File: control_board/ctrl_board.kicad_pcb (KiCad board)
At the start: 2 copper layers, 130 x 130 mm, 37 parts, among them J1 CONN_01X04, J2 CONN_01X02, J3 CONN_01X04, J4 CONN_01X04, J5 CONN_01X04, J6 CONN_01X04, J7 CONN_01X04, J8 CONN_01X04, U1 PCA9685PW, U2 MBI1801, U3 MBI1801, U4 MBI1801, U5 MBI1801, U6 MBI1801, U7 MBI1801

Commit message: ctrl_board: [wip] place and route
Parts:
- C11, C13, C3, C5, C7, C9: value 100n -> 100u
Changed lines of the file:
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@@
     (visible_elements FFFFBF7F)
     (pcbplotparams
-      (layerselection 0x00030_ffffffff)
+      (layerselection 0x010fc_ffffffff)
       (usegerberextensions false)
       (excludeedgelayer true)
-      (linewidth 0.150000)
+      (linewidth 0.020000)
       (plotframeref false)
       (viasonmask false)
@@
       (drillshape 0)
       (scaleselection 1)
-      (outputdirectory ""))
+      (outputdirectory gerbers/))
   )
   (net 0 "")
@@
       (effects (font (size 1 1) (thickness 0.15)))
     )
-    (fp_text value 100n (at 1 3.06 180) (layer F.Fab) hide
+    (fp_text value 100u (at 1 3.06 180) (layer F.Fab) hide
       (effects (font (size 1 1) (thickness 0.15)))
     )
@@
       (effects (font (size 1 1) (thickness 0.15)))
     )
-    (fp_text value 100n (at 1 3.06 120) (layer F.Fab) hide
+    (fp_text value 100u (at 1 3.06 120) (layer F.Fab) hide
       (effects (font (size 1 1) (thickness 0.15)))
     )
@@
       (effects (font (size 1 1) (thickness 0.15)))
     )
-    (fp_text value 100n (at 1 3.06 240) (layer F.Fab) hide
+    (fp_text value 100u (at 1 3.06 240) (layer F.Fab) hide
       (effects (font (size 1 1) (thickness 0.15)))
     )
@@
       (effects (font (size 1 1) (thickness 0.15)))
     )
-    (fp_text value 100n (at 1 3.06 300) (layer F.Fab) hide
+    (fp_text value 100u (at 1 3.06 300) (layer F.Fab) hide
       (effects (font (size 1 1) (thickness 0.15)))
     )
@@
       (effects (font (size 1 1) (thickness 0.15)))
     )
-    (fp_text value 100n (at 1 3.06) (layer F.Fab) hide
+    (fp_text value 100u (at 1 3.06) (layer F.Fab) hide
       (effects (font (size 1 1) (thickness 0.15)))
     )
@@
       (effects (font (size 1 1) (thickness 0.15)))
     )
-    (fp_text value 100n (at 1 3.06 60) (layer F.Fab) hide
-      (effects (font (size 1 1) (thickness 0.15)))
-    )
+    (fp_text value 100u (at 1 3.06 60) (layer F.Fab) hide
+      (effects (font (size 1 1) (thickness 0.15)))
+    )

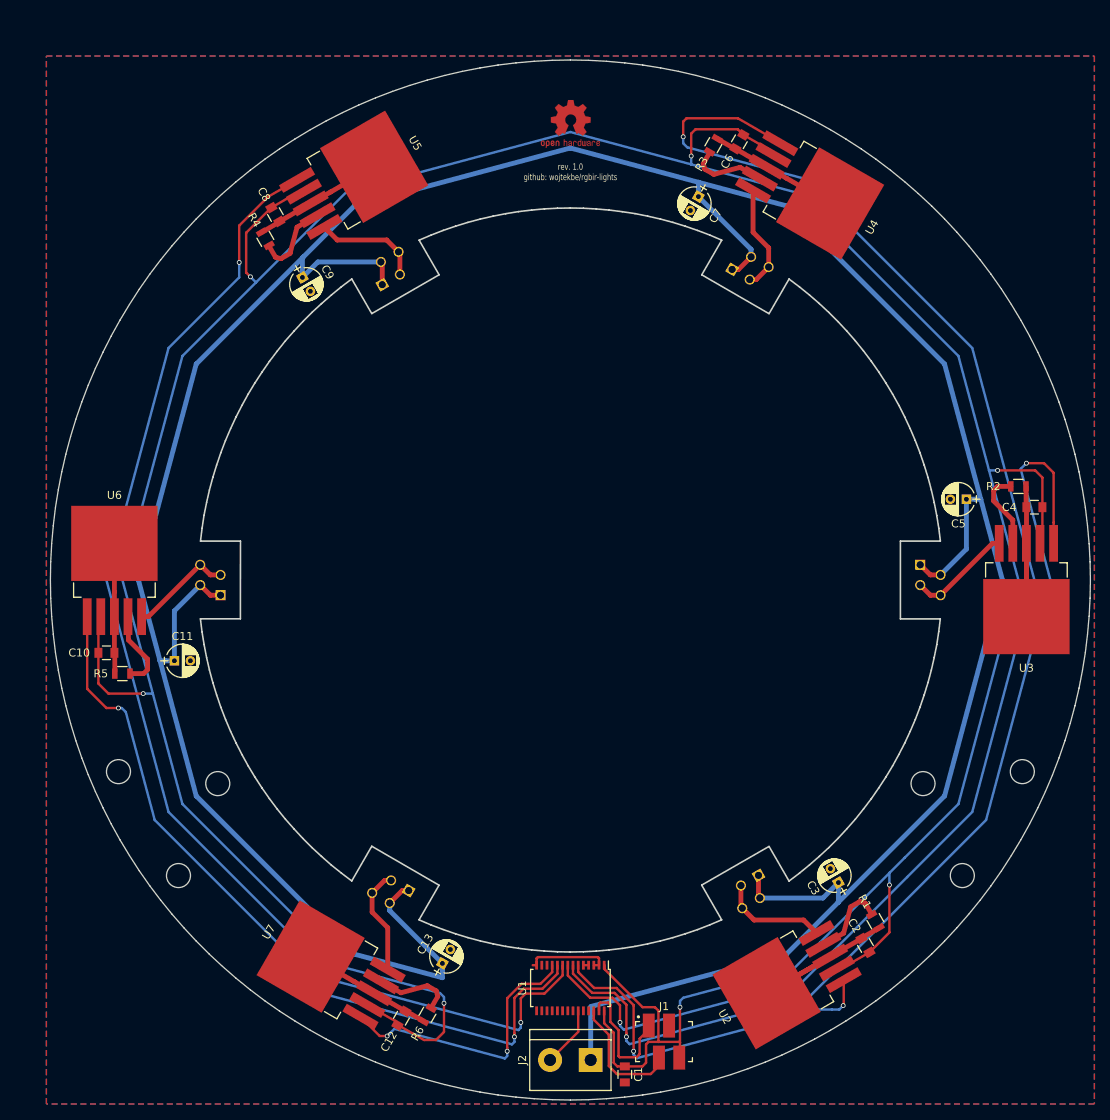
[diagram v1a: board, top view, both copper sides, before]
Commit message: ctrl_board: fixes: PCA9685, MBI1801 package
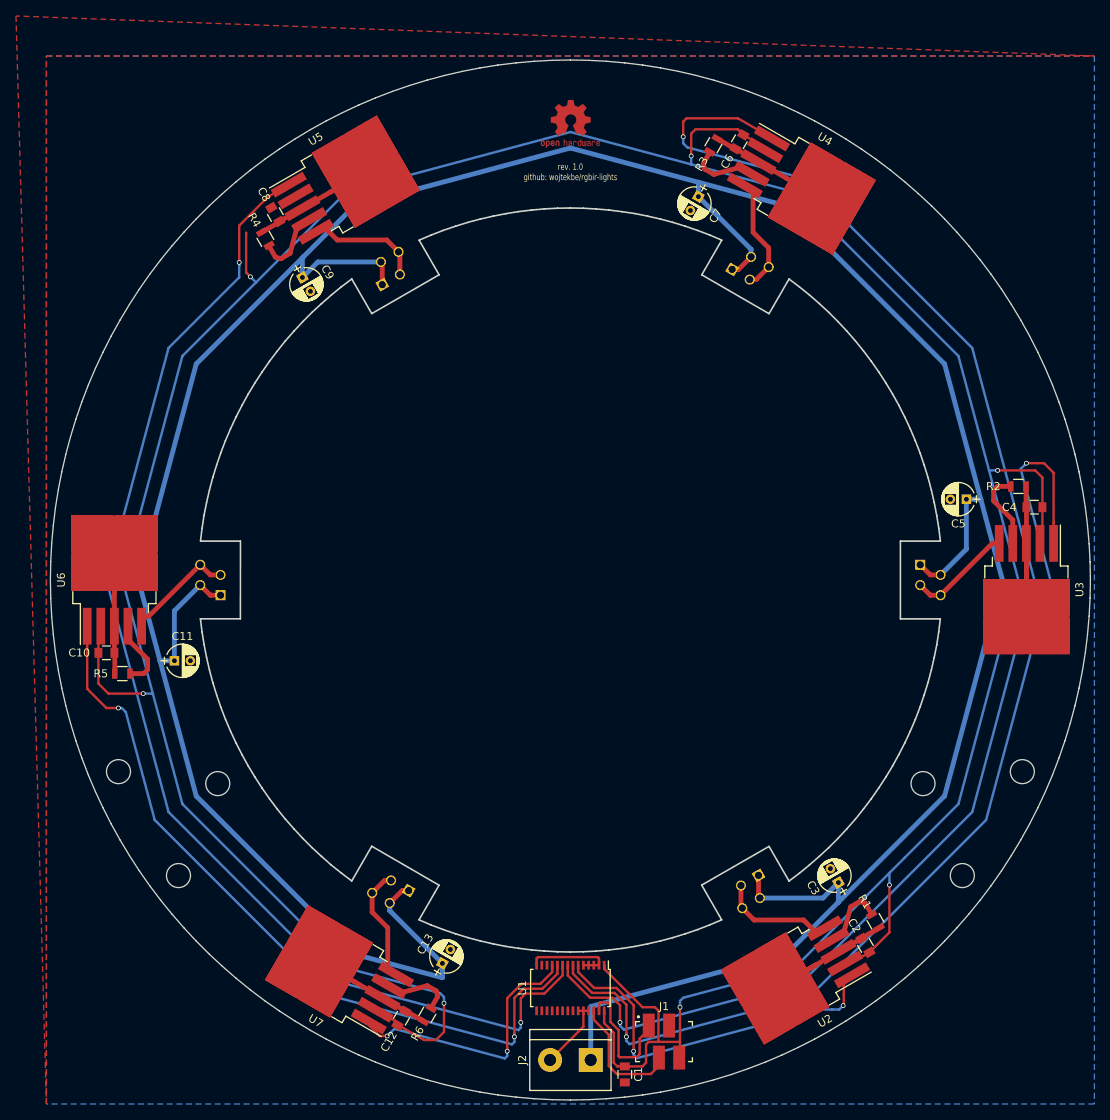
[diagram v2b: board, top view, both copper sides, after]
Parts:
- U2, U3, U4, U5, U6, U7: footprint TO_SOT_Packages_SMD:TO-263-5Lead -> TO_SOT_Packages_SMD:TO-263-5_TabPin3
- moved U3 1.20 mm to (57.0, 1.20)
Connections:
- U1 pad 24: (no net) -> GND
- U1 pad 25: (no net) -> GND
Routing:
- net +5V: track 448.3 -> 439.7 mm
- net GND: track 131.8 -> 133.5 mm

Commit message: control board: rev1.1: place and route
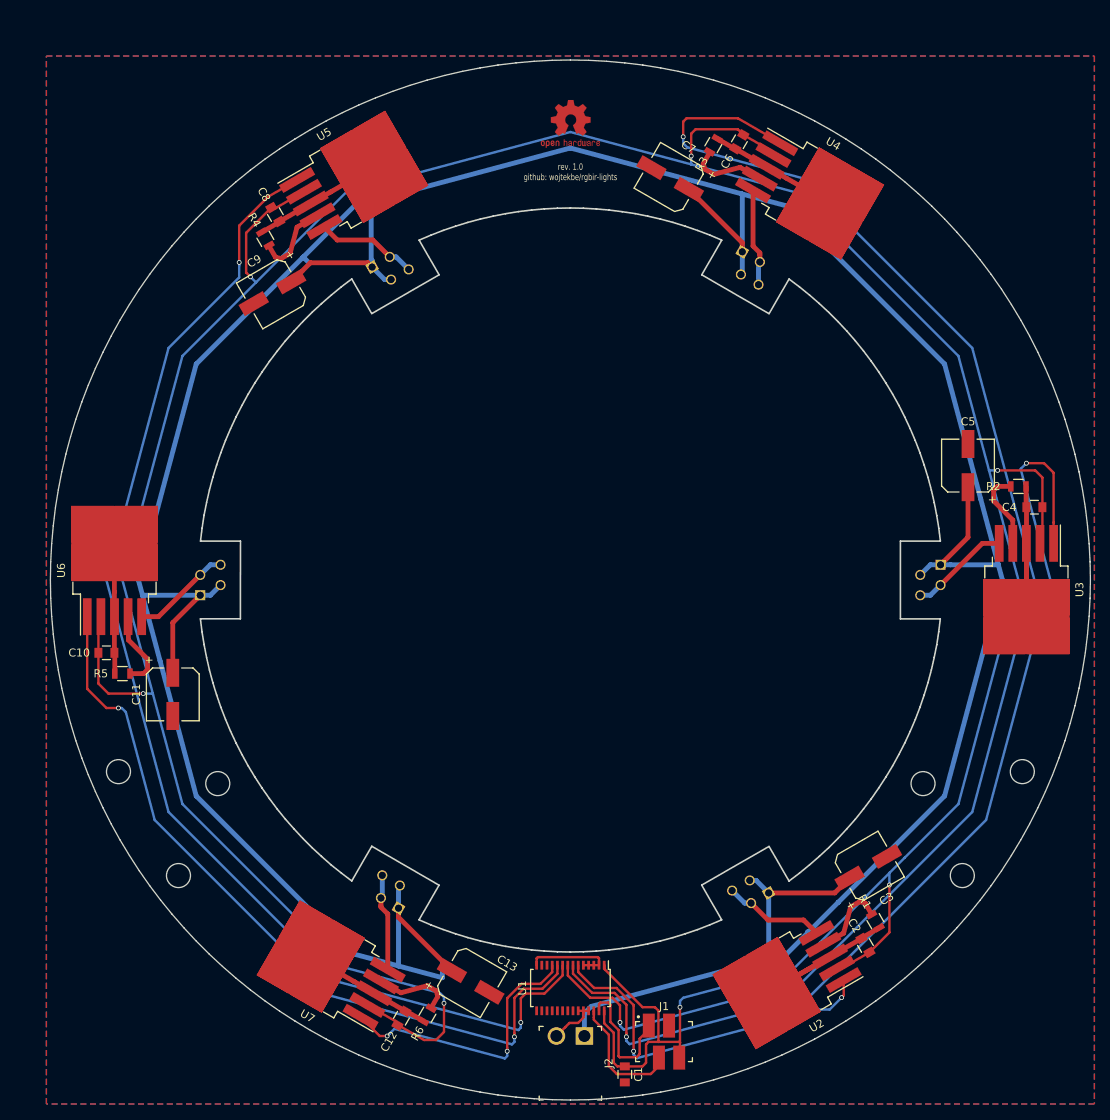
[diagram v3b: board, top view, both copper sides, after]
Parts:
- C11, C13, C3, C5, C7, C9: footprint Capacitors_THT:CP_Radial_D4.0mm_P2.00mm -> Capacitors_SMD:CP_Elec_6.3x5.3
- J2: footprint Connectors:bornier2 -> generated:THT_15EDGRC_2p
- moved C11 4.20 mm to (-49.7, 14.3), turned to 270 degrees
- moved C5 4.20 mm to (49.7, -14.3), turned to 90 degrees
- moved C3 4.20 mm to (37.2, 35.9), turned to 30 degrees
- moved C9 4.20 mm to (-37.2, -35.9), turned to 210 degrees
- moved C13 4.20 mm to (-12.5, 50.2), turned to 330 degrees
- moved C7 4.20 mm to (12.5, -50.2), turned to 150 degrees
- moved J2 2.57 mm to (0.00, 60.4)
- moved U2 1.20 mm to (27.5, 50.0)
- moved U5 1.20 mm to (-27.5, -50.0)
- moved U4 1.19 mm to (29.5, -48.8)
- moved U7 1.19 mm to (-29.5, 48.8)
- moved U6 1.19 mm to (-57.0, -1.19)
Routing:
- net VLED: track 416.5 -> 452.5 mm
- net +5V: track 439.7 -> 448.3 mm
- net GND: track 133.5 -> 130.8 mm
- net N$5: track 13.4 -> 12.2 mm
- net N$11: track 13.4 -> 12.2 mm
- net N$1: track 13.5 -> 12.7 mm
- net N$7: track 13.5 -> 12.7 mm
- net CTRL1: track 46.3 -> 45.6 mm
- net N$9: track 13.2 -> 12.5 mm
- net N$3: track 13.1 -> 12.6 mm
